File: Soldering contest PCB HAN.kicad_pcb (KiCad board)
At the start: 2 copper layers, 99.1 x 98.6 mm, 19 parts, among them J1 Screw_Terminal_01x02, Q1 BC817, Q2 2N3904

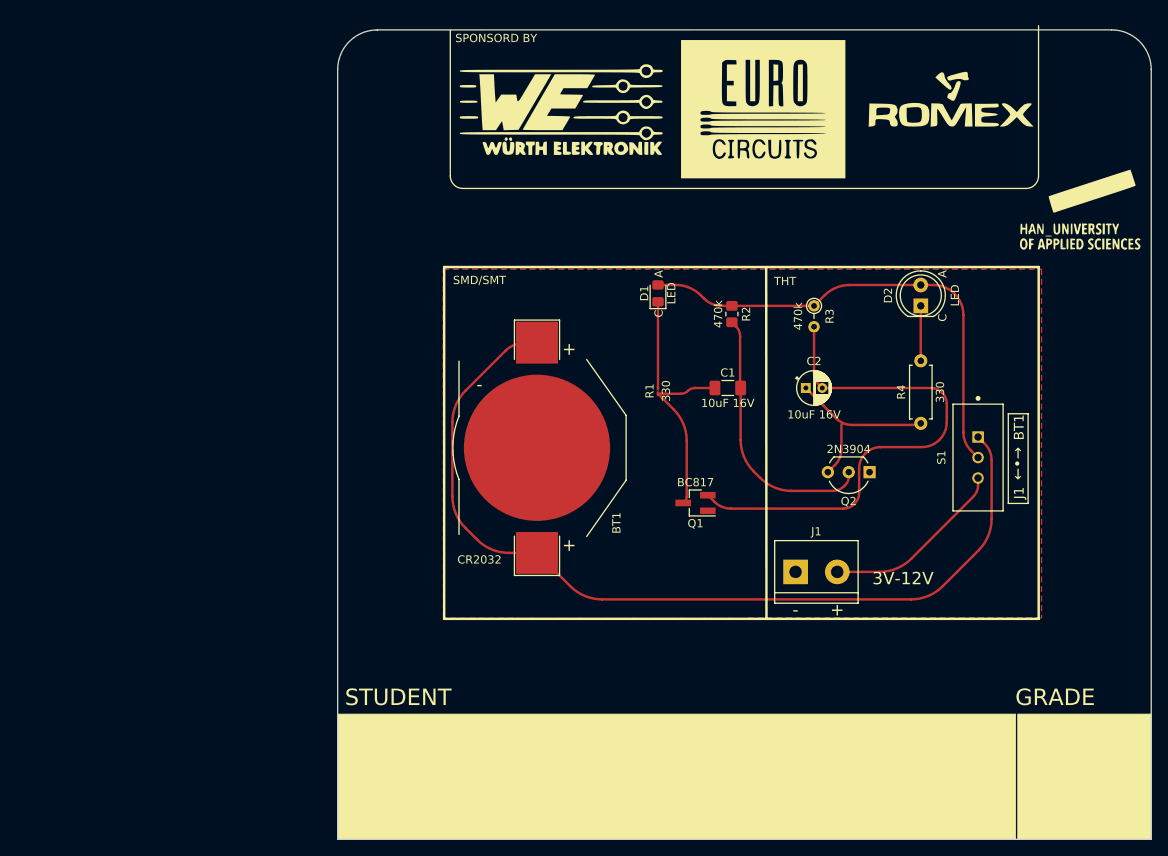
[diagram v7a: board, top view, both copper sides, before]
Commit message: enh board
-added mounting holes
-updated silkscreen date
-changed R1 footprint to match ERC
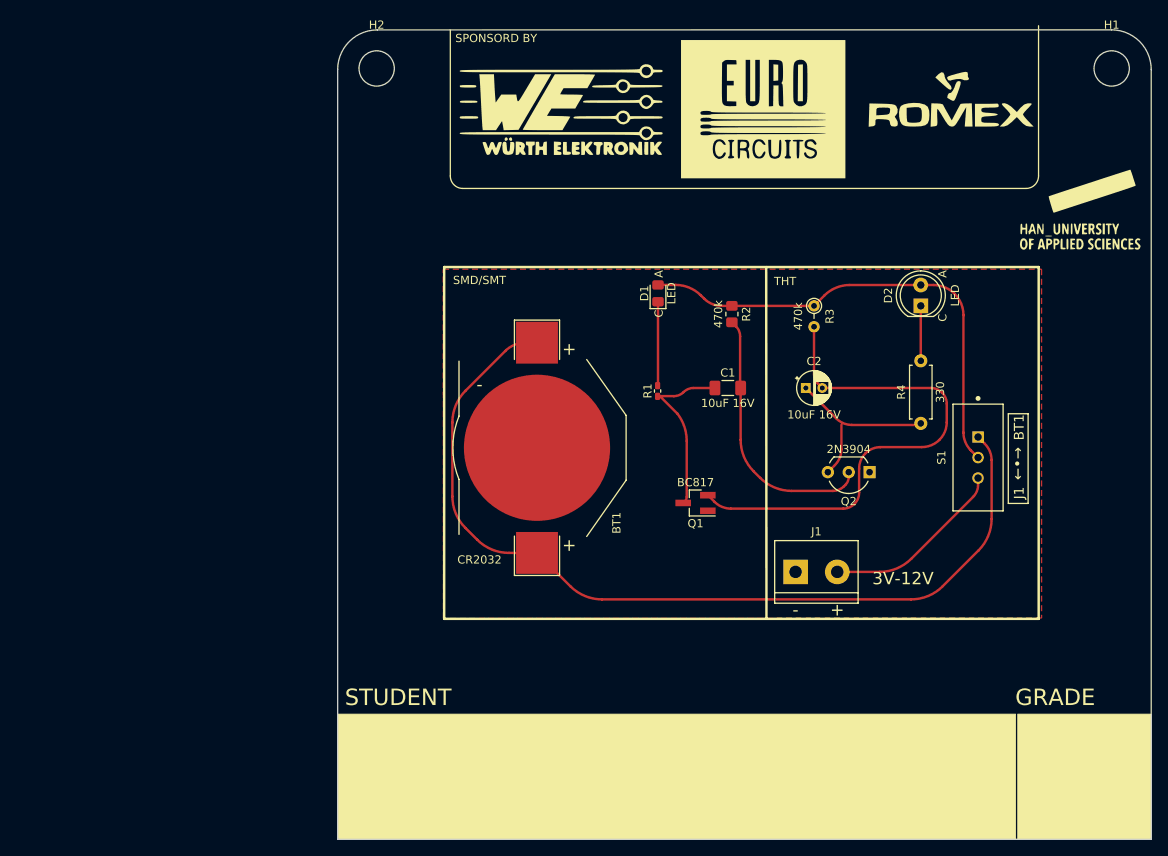
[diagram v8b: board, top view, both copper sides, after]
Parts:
- removed REF**: KiCad-Logo2_12mm_SilkScreen, Symbol:KiCad-Logo2_12mm_SilkScreen
- added H1: MountingHole, MountingHole:MountingHole_4.3mm_M4, F.Cu at (205.5, 56.0)
- added H2: MountingHole, MountingHole:MountingHole_4.3mm_M4, F.Cu at (116.0, 56.0)
- R1: footprint Resistor_SMD:R_01005_0402Metric_Pad0.57x0.30mm_HandSolder -> Resistor_SMD:R_0402_1005Metric
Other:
- board text added: "Project: Astable multivibrator Version: 0.3 Date: 28-11-2022 Documentation: https://gitlab.com/wlgrw/2023-ese-day-soldering-contest.git Designed for: ESE-day 27 January 2023 soldering contest Designed by: Casper R. Tak"
- board text removed: "Project: Astable multivibrator Version: 0.2 Date: 18-11-2022 Documentation: https://gitlab.com/wlgrw/2023-ese-day-soldering-contest.git Designed for: ESE-day 27 January 2023 soldering contest Designed by: Casper R. Tak"
